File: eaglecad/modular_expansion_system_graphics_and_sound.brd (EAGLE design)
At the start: 90.2 x 100 mm, 44 parts, among them IC1 74LS244N, IC8 74LS244N, IC9-74HCU04 74LS04N, J1-WAIT-AND-INT WAIT-AND-INT, J1_ADDRESS_CON j1, J2_DATA_AND_POWER_CON j2, J3-VIDEO-OUT RCA, J4-AUDIO-LEFT RCA, J5-AUDIO-RIGHT RCA, Q2 2N2222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

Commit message: added text to boards
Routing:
- net D3: track 141.4 -> 143.8 mm
- net DOWN: track 50.1 -> 48.7 mm
- net TRIGGER: track 67.3 -> 66.2 mm
- net N$1: track 15.6 -> 16.4 mm
- net VDP-RD1: track 48.4 -> 49.1 mm
- net TMS9918_AD5-TMS4416_A2: track 68.1 -> 67.5 mm
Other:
- board text added: "TRS80MXS Gfx/Snd V1.0 Joe Rounceville (C) 2019"

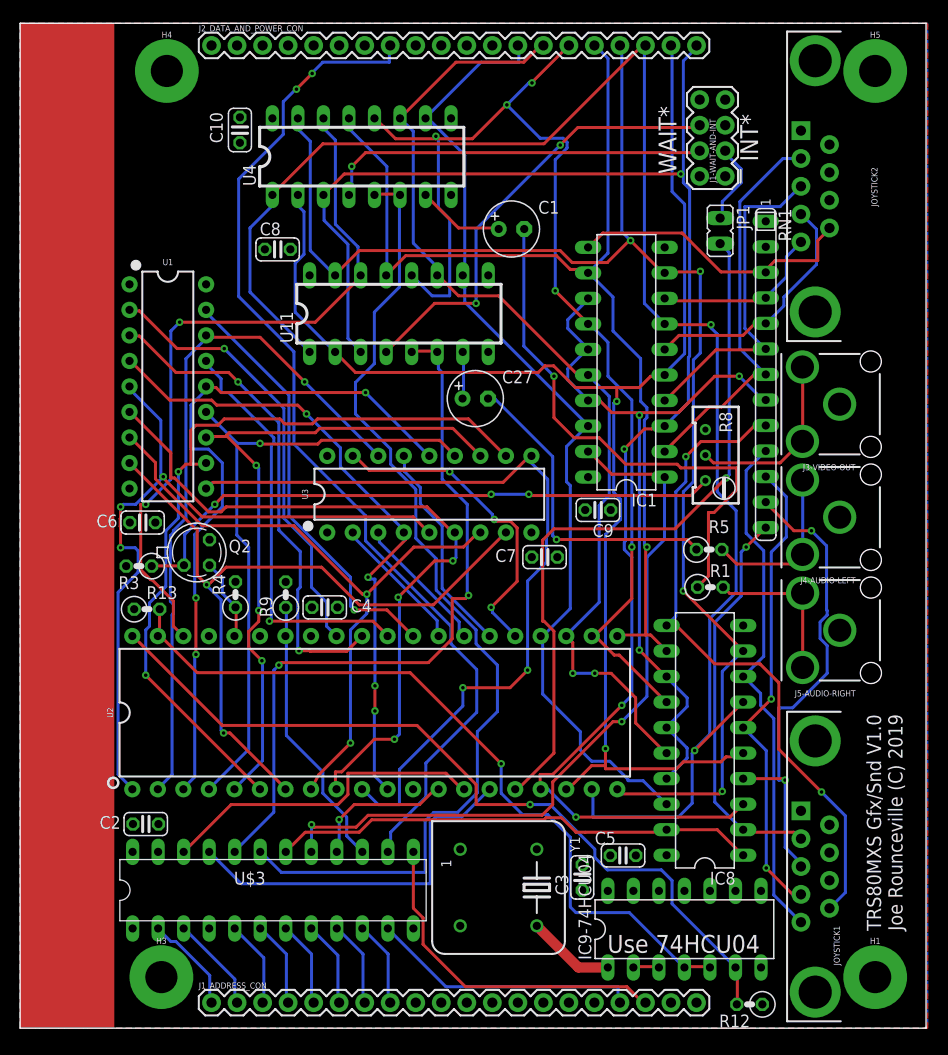
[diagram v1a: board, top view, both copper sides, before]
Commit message: removed soft reset for vdp, added 12 voice sound
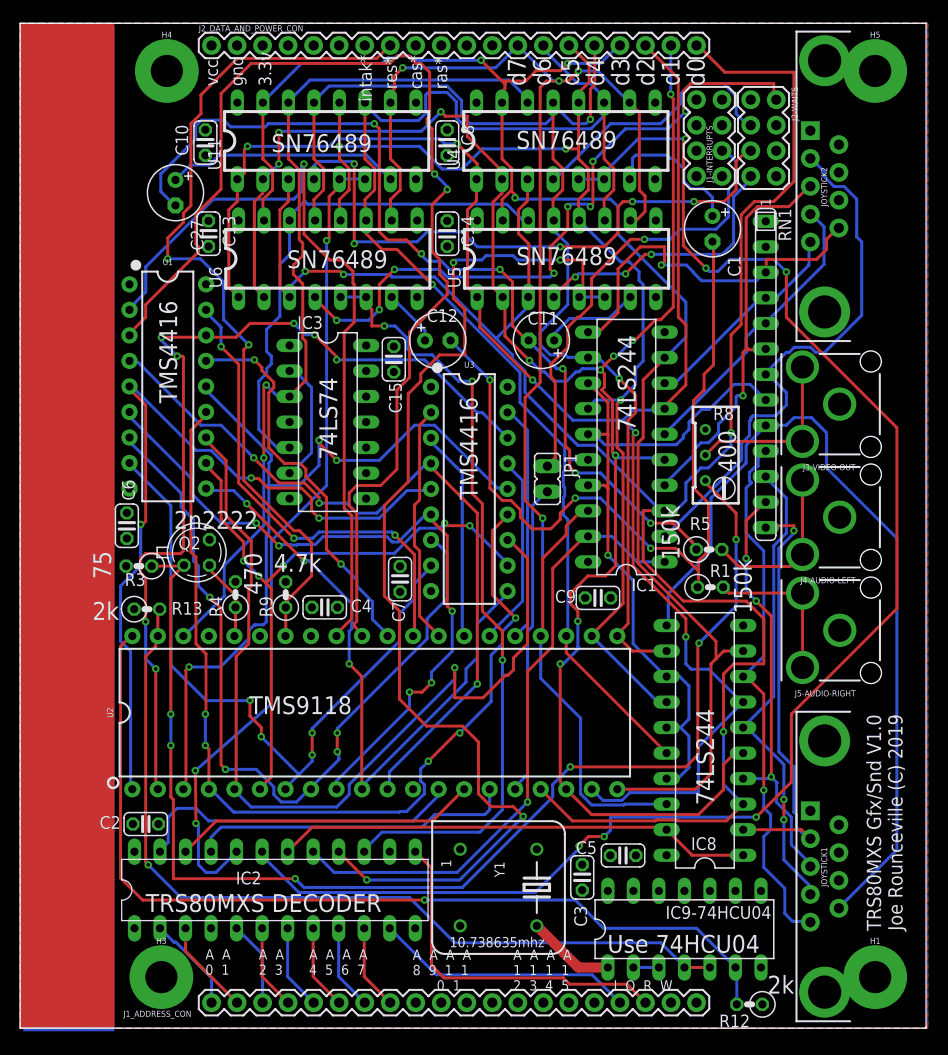
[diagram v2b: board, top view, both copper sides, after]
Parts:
- removed J1-WAIT-AND-INT: WAIT-AND-INT, SparkFun-Connectors:2X4
- removed U$3: TRS80GS_DECODER, TMS99:DIP24SKI
- added C11, C12: 10uf, resistor:E2,5-6
- added C13, C14, C15: .1uf, resistor:C025-024X044
- added IC2: ATF22V10, TMS99:DIP24SKI
- added IC3: 74LS74N, 74xx-us:DIL14
- added J1-INTERRUPTS: INTERRUPTS, SparkFun-Connectors:2X4
- added J2-WAITS: WAITS, SparkFun-Connectors:2X4
- added U5, U6: SN76489, TMS99:DIP16
- C10, C2, C3, C4, C5, C6, C7, C8, C9: value (none) -> .1uf
- moved C27 36.2 mm to (15.5, 83.1), turned to 270 degrees
- moved JP1 30.1 mm to (52.5, 54.7)
- moved U4 20.4 mm to (54.3, 88.3)
- moved C1 20.0 mm to (68.9, 79.5), turned to 270 degrees
- moved C8 19.9 mm to (42.5, 88.1), turned to 270 degrees
- moved U11 18.6 mm to (30.5, 88.3)
- moved C7 14.5 mm to (37.8, 44.7), turned to 90 degrees
- moved C9 8.75 mm to (57.5, 42.8)
- moved IC1 8.44 mm to (60.3, 57.8)
- moved U3 4.01 mm to (44.7, 53.7), turned to 270 degrees
- moved C10 3.66 mm to (18.4, 88.1)
- moved C6 1.59 mm to (10.6, 50.0), turned to 270 degrees
- moved JOYSTICK1 0.94 mm to (80.1, 16.1)
- moved JOYSTICK2 0.94 mm to (80.1, 83.8)
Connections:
- removed net VID_RESET*: R9.1, U$3.15, U2.P34
- new net CLOCK_DIV_2: IC3.5, U5.P14, U6.P14
- new net CSR: IC2.21, U2.P15
- new net CSW: IC2.22, U2.P14
- new net N$10: C11.+, U5.P7
- new net N$11: IC2.15, U6.P5, U6.P6
- new net N$13: C12.+, U6.P7
- new net N$8: J2-WAITS.7, U5.P4
- new net N$9: IC2.16, U5.P5, U5.P6
- net A0: now also IC2.2; no longer U$3.2
- net A1: now also IC2.3; no longer U$3.3
- net A2: now also IC2.5; no longer U$3.5
- net A3: now also IC2.6; no longer U$3.6
- net A4: now also IC2.7; no longer U$3.7
- net A5: now also IC2.8; no longer U$3.8
- net A6: now also IC2.9; no longer U$3.9
- net A7: now also IC2.10; no longer U$3.10
- net D0: now also U5.P3, U6.P3
- net D1: now also U5.P2, U6.P2
- net D2: now also U5.P1, U6.P1
- net D3: now also U5.P15, U6.P15
- net D4: now also U5.P13, U6.P13
- net D5: now also U5.P12, U6.P12
- net D6: now also U5.P11, U6.P11
- net D7: now also U5.P10, U6.P10
- net GND: now also C13.2, C14.2, C15.2, IC2.12, IC3.10, IC3.11, IC3.12, IC3.13, IC3.7, U5.P8, U6.P8; no longer U$3.12
- net IN*: now also IC2.11; no longer U$3.11
- net JOY1_IN_ENABLE_N: now also IC2.18; no longer U$3.18
- net JOY1_IN_ENABLE_N1: now also IC2.17; no longer U$3.17
- net N$14: now also IC3.2, IC3.6; no longer U$3.22, U2.P14
- net N$15: now also J2-WAITS.2, U6.P4; no longer U$3.21, U2.P15
- net N$2: now also J1-INTERRUPTS.3; no longer J1-WAIT-AND-INT.3
- net N$5: now also C12.-
- net N$64: now also C11.-
- net OUT*: now also IC2.13; no longer U$3.13
- net SN76489-CLOCK: now also IC3.3
- net SND1_ENABLE_N: now also IC2.20; no longer U$3.20
- net SND1_READY: now also J2-WAITS.5; no longer J1-WAIT-AND-INT.6
- net SND2_ENABLE_N: now also IC2.19; no longer U$3.19
- net SND2_READY: now also J2-WAITS.3; no longer J1-WAIT-AND-INT.4
- net SYSRES*: now also R9.1, U2.P34; no longer U$3.14
- net VCC: now also C13.1, C14.1, C15.1, IC2.24, IC3.1, IC3.14, IC3.4, U5.P16, U6.P16; no longer U$3.24
- net VDP_MODE: now also IC2.23; no longer U$3.16
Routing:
- net N$9: track 0.00 -> 111.3 mm, vias 0 -> 4
- net N$11: track 0.00 -> 78.1 mm, vias 0 -> 3
- net VDP-RD1: track 49.1 -> 115.5 mm
- net COMVID-OUT: track 60.5 -> 124.0 mm, vias 3 -> 6
- net N$64: track 31.6 -> 92.3 mm, vias 1 -> 6
- net D7: track 98.6 -> 156.1 mm, vias 0 -> 4
- net SND2_ENABLE_N: track 99.3 -> 156.4 mm, vias 0 -> 6
- net CLOCK_DIV_2: track 0.00 -> 51.9 mm
- net D0: track 159.2 -> 209.1 mm
- net N$3: track 71.7 -> 31.0 mm, vias 1 -> 0
- net D1: track 145.8 -> 184.7 mm, vias 2 -> 11
- net N$2: track 8.27 -> 45.0 mm, vias 0 -> 1
- net D6: track 100.2 -> 134.2 mm, vias 2 -> 1
- net VDP-RD0: track 44.3 -> 77.7 mm
- net TMS9918_AD6-TMS4416_A1: track 63.5 -> 95.9 mm, vias 1 -> 5
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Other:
- board text added: "10.738635mhz"
- board text added: "150k"
- board text added: "2k"
- board text added: "2n2222"
- board text added: "3.3v"
- board text added: "4.7k"
- board text added: "400"
- board text added: "470"
- board text added: "74LS244"
- board text added: "74LS74"
- board text added: "75"
- board text added: "A A 0 1"
- board text added: "A A 2 3"
- board text added: "A A A A 1 1 1 1 2 3 4 5"
- board text added: "A A A A 4 5 6 7"
- board text added: "A A A A 8 9 1 1 0 1"
- board text added: "I O R W"
- board text added: "SN76489"
- board text added: "TMS4416"
- board text added: "TMS9118"
- board text added: "TRS80MXS DECODER"
- board text added: "cas*"
- board text added: "d0"
- board text added: "d1"
- board text added: "d2"
- board text added: "d3"
- board text added: "d4"
- board text added: "d5"
- board text added: "d6"
- board text added: "d7"
- board text added: "gnd"
- board text added: "intak*"
- board text added: "ras*"
- board text added: "res*"
- board text added: "vcc"
- board text removed: "INT*"
- board text removed: "WAIT*"

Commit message: updated readme
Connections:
- removed net CLOCK_DIV_2: IC3.5, U5.P14, U6.P14
- new net CLOCK_DIV_4: IC3.9, U5.P14, U6.P14
- new net N$6: IC3.11, IC3.5
- new net N$7: IC3.12, IC3.8
- net GND: no longer IC3.10, IC3.11, IC3.12, IC3.13
- net VCC: now also IC3.10, IC3.13
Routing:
- net CLOCK_DIV_4: track 0.00 -> 62.4 mm, vias 0 -> 1
- net CLOCK_DIV_2: track 51.9 -> 0.00 mm
- net N$7: track 0.00 -> 11.9 mm, vias 0 -> 1
- net N$6: track 0.00 -> 10.3 mm, vias 0 -> 1
- net TMS9918_AD7-TMS4416_A0: track 81.0 -> 85.6 mm
- net DOWN: track 43.8 -> 42.7 mm
- net D5: track 119.2 -> 118.7 mm

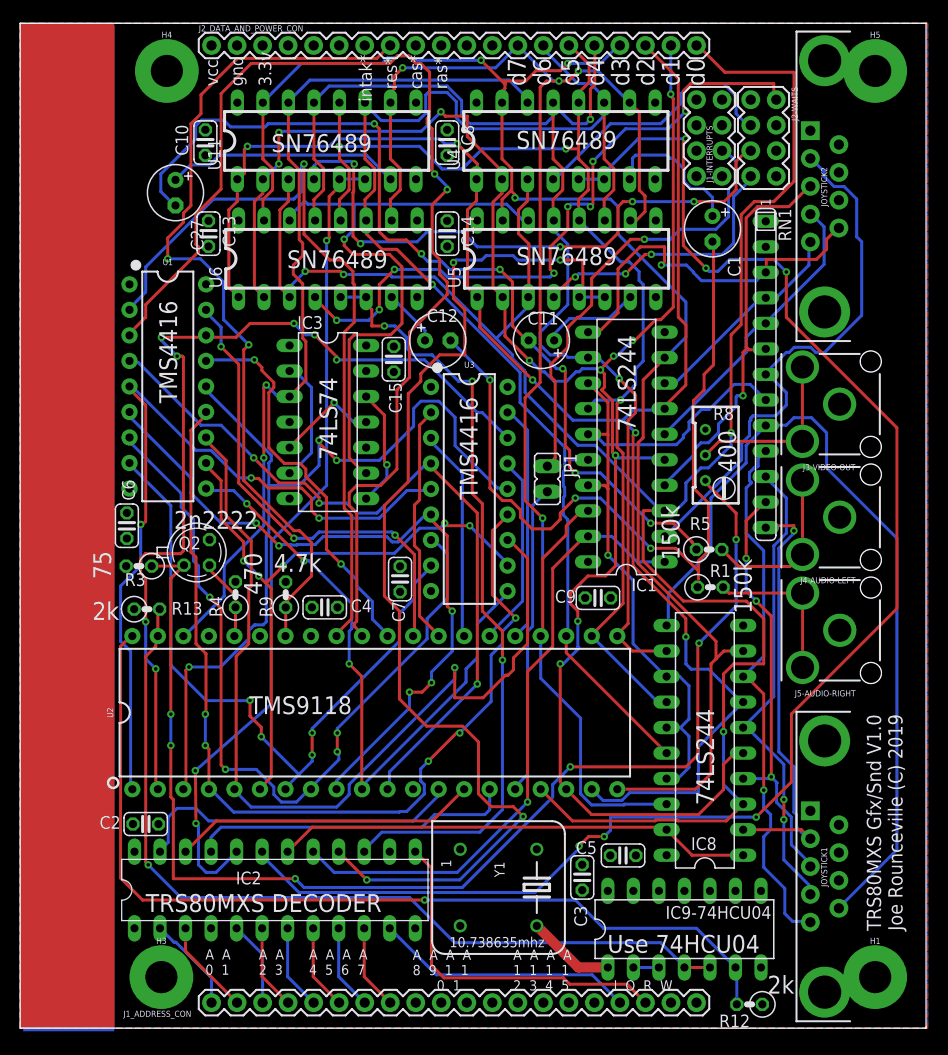
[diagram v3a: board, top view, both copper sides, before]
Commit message: tweaked sound circuit
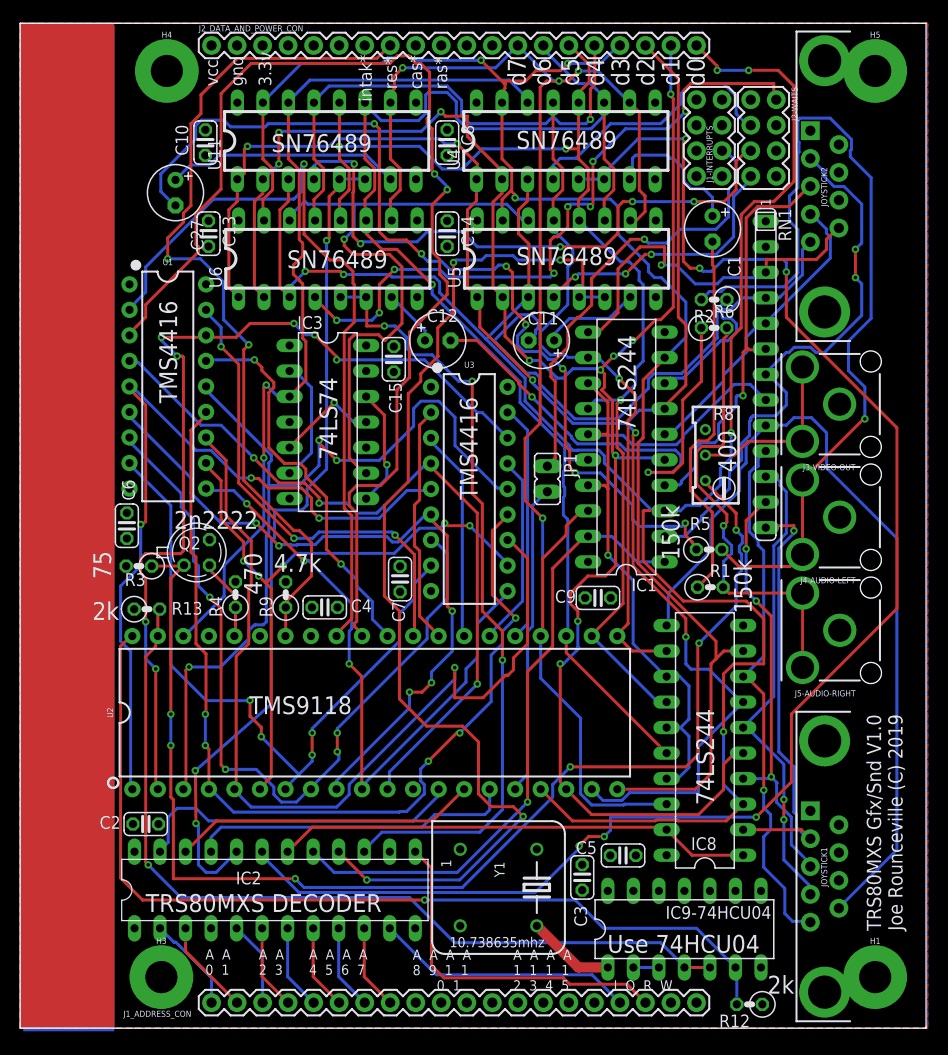
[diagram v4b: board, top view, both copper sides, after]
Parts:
- added R2, R6: 150k, resistor:0207/2V
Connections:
- new net N$16: C1.-, R1.1
- new net N$17: C11.-, R2.1
- net N$1: now also R2.2
- net N$24: now also R6.2
- net N$5: now also R6.1; no longer C1.-, R1.1
- net N$64: no longer C11.-
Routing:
- net N$1: track 16.6 -> 88.7 mm, vias 0 -> 1
- net N$17: track 0.00 -> 41.9 mm
- net N$16: track 0.00 -> 37.5 mm
- net N$24: track 15.6 -> 45.8 mm, vias 0 -> 1
- net N$5: track 80.2 -> 50.3 mm, vias 3 -> 2
- net N$64: track 92.3 -> 96.5 mm, vias 6 -> 7
- net RIGHT1: track 21.6 -> 25.5 mm
- net N$9: track 111.3 -> 108.9 mm
- net UP1: track 54.3 -> 56.0 mm, vias 0 -> 2
- net D0: track 209.1 -> 210.8 mm, vias 4 -> 6
- net SND1_ENABLE_N: track 82.1 -> 83.7 mm
- net SND2_ENABLE_N: track 156.4 -> 157.8 mm
- net DOWN1: track 40.8 -> 42.0 mm
- net LEFT1: track 29.4 -> 30.3 mm
- net SND2_READY: track 27.0 -> 27.8 mm
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
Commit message: boards as they were when sent to allpcb
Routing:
- net TMS9918_AD7-TMS4416_A0: track 85.6 -> 89.4 mm
- net TMS9918_AD4-TMS4416_A3: track 64.1 -> 66.9 mm
- net D6: track 134.2 -> 135.7 mm
- net TMS9918_AD5-TMS4416_A2: track 91.9 -> 90.7 mm
- net N$21: track 90.7 -> 89.7 mm
- net LEFT: track 47.8 -> 48.8 mm
- net N$17: track 41.9 -> 41.0 mm
- net CSR: track 32.3 -> 33.2 mm
- net N$15: track 68.5 -> 69.3 mm
- net TMS9918_AD1-TMS4416_A6: track 72.2 -> 71.4 mm
- net SND2_ENABLE_N: track 157.8 -> 158.6 mm
- net SND1_ENABLE_N: track 83.7 -> 84.4 mm
- net TMS9918_AD6-TMS4416_A1: track 95.7 -> 96.4 mm
- net VDP-RD1: track 115.5 -> 114.8 mm
- net TMS9918_AD0-TMS4416_A7: track 64.0 -> 64.7 mm
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
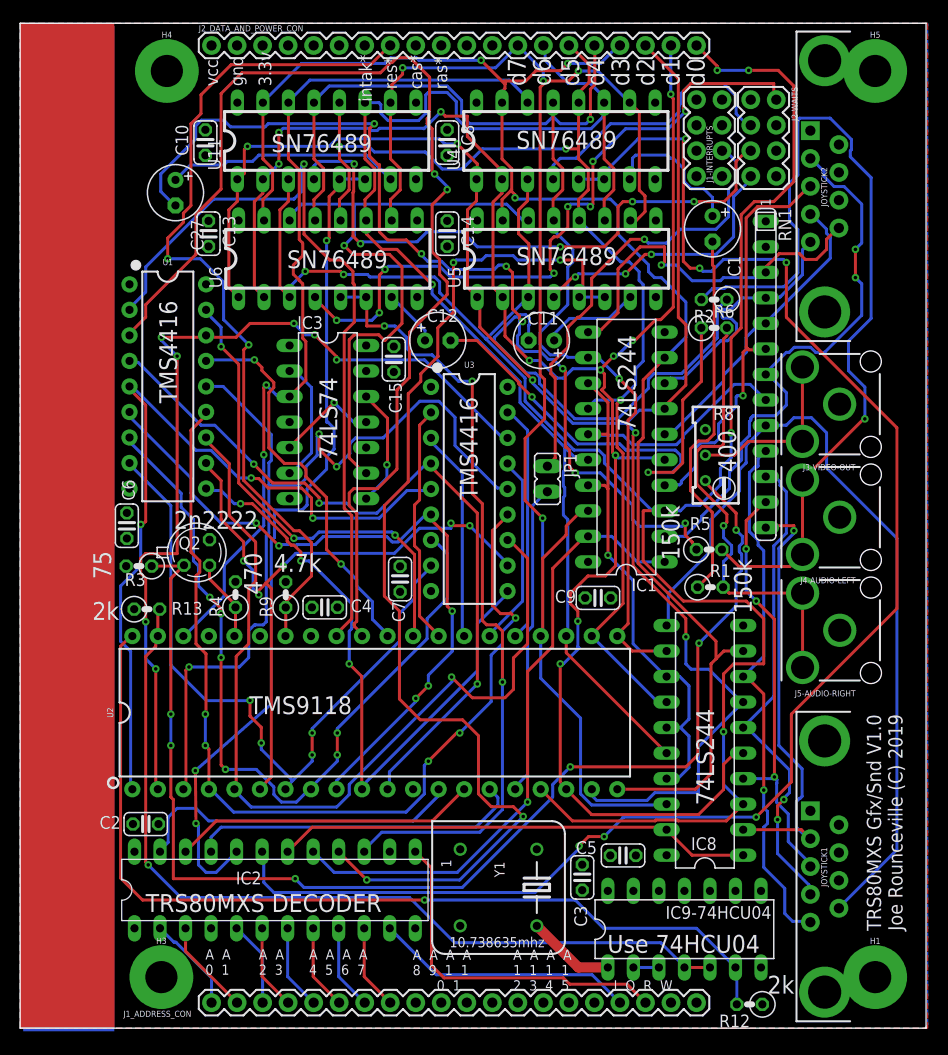
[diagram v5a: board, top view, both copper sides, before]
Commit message: updated sound board, fixed mirrored headers
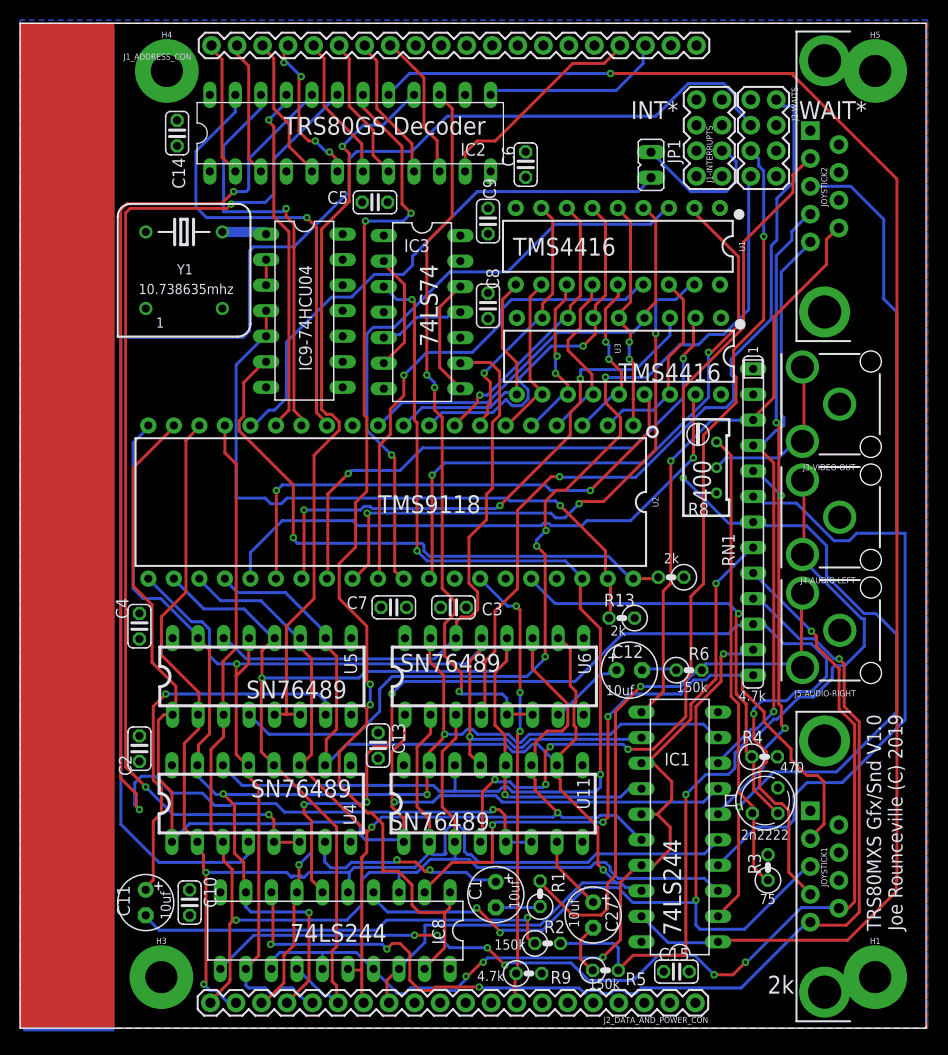
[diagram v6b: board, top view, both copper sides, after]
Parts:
- moved J2_DATA_AND_POWER_CON 106.7 mm to (67.2, 2.52), turned to 180 degrees
- moved J1_ADDRESS_CON 95.2 mm to (19.1, 97.8)
- moved C27 83.0 mm to (57.0, 11.3)
- moved IC2 75.7 mm to (30.3, 89.1)
- moved C10 75.6 mm to (16.9, 12.5), turned to 90 degrees
- moved U4 72.6 mm to (24.0, 22.4)
- moved IC9-74HCU04 72.2 mm to (28.3, 71.4), turned to 270 degrees
- moved C1 69.7 mm to (47.3, 13.3)
- moved C5 69.5 mm to (35.3, 82.2), turned to 0 degrees
- moved R3 69.4 mm to (74.4, 16.0), turned to 90 degrees
- moved Y1 68.9 mm to (16.3, 75.4), turned to 0 degrees
- moved C11 68.4 mm to (12.5, 12.5), turned to 270 degrees
- moved U11 68.0 mm to (47.1, 22.4)
- moved C15 67.1 mm to (65.3, 5.62), turned to 0 degrees
- moved R2 66.2 mm to (52.5, 8.44), turned to 0 degrees
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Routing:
- net SND2_READY: track 28.2 -> 146.6 mm
- net JOY1_IN_ENABLE_N1: track 63.0 -> 155.5 mm
- net N$64: track 96.9 -> 5.30 mm, vias 7 -> 0
- net COMVID-OUT: track 124.7 -> 45.9 mm, vias 6 -> 0
- net TMS9918_AD6-TMS4416_A1: track 96.4 -> 18.1 mm, vias 5 -> 0
- net D0: track 210.7 -> 132.5 mm, vias 6 -> 1
- net TMS9918_AD5-TMS4416_A2: track 90.7 -> 17.0 mm, vias 1 -> 2
- net TMS9918_AD7-TMS4416_A0: track 89.4 -> 17.4 mm, vias 3 -> 2
- net N$8: track 27.2 -> 98.2 mm, vias 3 -> 4
- net N$21: track 89.7 -> 19.7 mm, vias 7 -> 0
- net DOWN1: track 42.0 -> 102.3 mm, vias 1 -> 0
- net JOY1_IN_ENABLE_N: track 47.5 -> 106.9 mm, vias 0 -> 4
- net LEFT: track 48.8 -> 108.1 mm, vias 2 -> 4
- net N$18: track 80.2 -> 23.4 mm, vias 3 -> 2
- net RIGHT: track 53.5 -> 109.6 mm, vias 1 -> 4
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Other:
- board text added: "10uf"
- board text added: "INT*"
- board text added: "TRS80GS Decoder"
- board text added: "WAIT*"
- board text removed: "3.3v"
- board text removed: "A A 0 1"
- board text removed: "A A 2 3"
- board text removed: "A A A A 1 1 1 1 2 3 4 5"
- board text removed: "A A A A 4 5 6 7"
- board text removed: "A A A A 8 9 1 1 0 1"
- board text removed: "I O R W"
- board text removed: "TRS80MXS DECODER"
- board text removed: "Use 74HCU04"
- board text removed: "cas*"
- board text removed: "d0"
- board text removed: "d1"
- board text removed: "d2"
- board text removed: "d3"
- board text removed: "d4"
- board text removed: "d5"
- board text removed: "d6"
- board text removed: "d7"
- board text removed: "gnd"
- board text removed: "intak*"
- board text removed: "ras*"
- board text removed: "res*"
- board text removed: "vcc"
